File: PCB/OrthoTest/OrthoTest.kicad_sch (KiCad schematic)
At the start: 249 parts, among them SW1 SW_Push, SW10 SW_Push, SW11 SW_Push, SW12 SW_Push, SW13 SW_Push, SW14 SW_Push, SW15 SW_Push, SW16 SW_Push, SW17 SW_Push, SW18 SW_Push, SW19 SW_Push, SW2 SW_Push, SW20 SW_Push, SW21 SW_Push, SW22 SW_Push, SW23 SW_Push, SW24 SW_Push, SW25 SW_Push, SW26 SW_Push, SW27 SW_Push, SW28 SW_Push, SW29 SW_Push, SW3 SW_Push, SW30 SW_Push, SW31 SW_Push, SW32 SW_Push, SW33 SW_Push, SW34 SW_Push, SW35 SW_Push, SW36 SW_Push, SW37 SW_Push, SW38 SW_Push, SW39 SW_Push, SW4 SW_Push, SW40 SW_Push, SW41 SW_Push, SW42 SW_Push, SW43 SW_Push, SW44 SW_Push, SW45 SW_Push, SW46 SW_Push, SW47 SW_Push, SW48 SW_Push, SW49 SW_Push, SW5 SW_Push, SW50 SW_Push, SW51 SW_Push, SW52 SW_Push, SW53 SW_Push, SW54 SW_Push, SW55 SW_Push, SW56 SW_Push, SW57 SW_Push, SW58 SW_Push, SW59 SW_Push, SW6 SW_Push, SW60 RotaryEncoder_Switch_MP, SW61 RotaryEncoder_Switch_MP, SW7 SW_Push, SW8 SW_Push, SW9 SW_Push

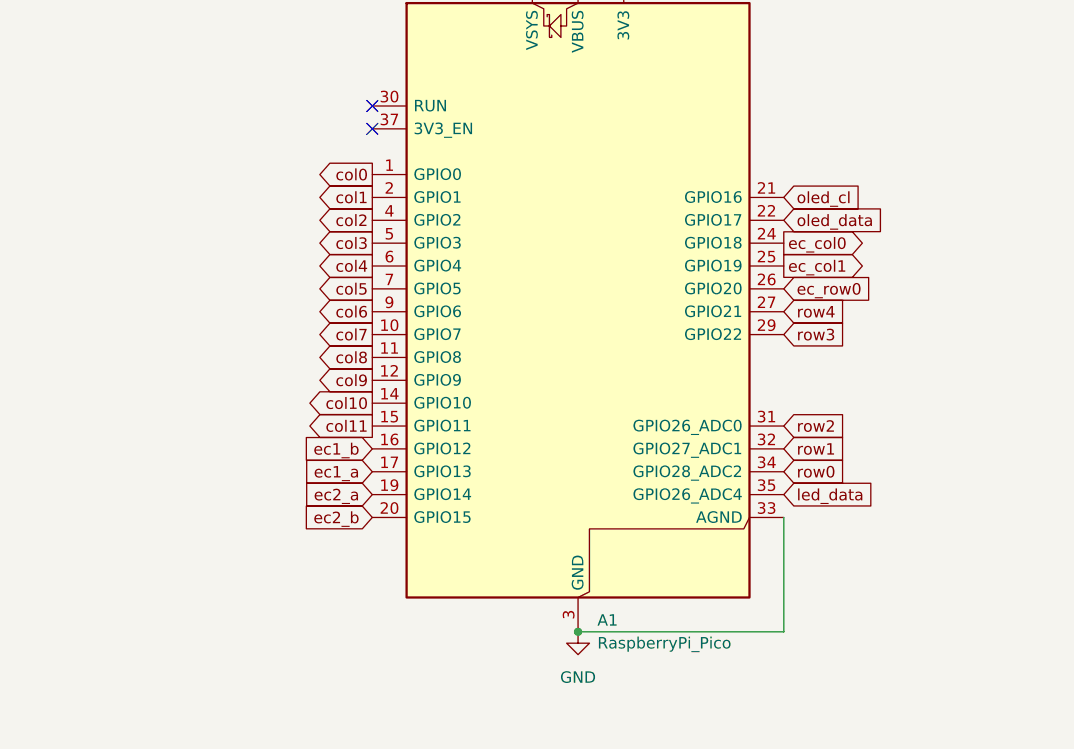
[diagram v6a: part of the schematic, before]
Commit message: rerouting ucontroller
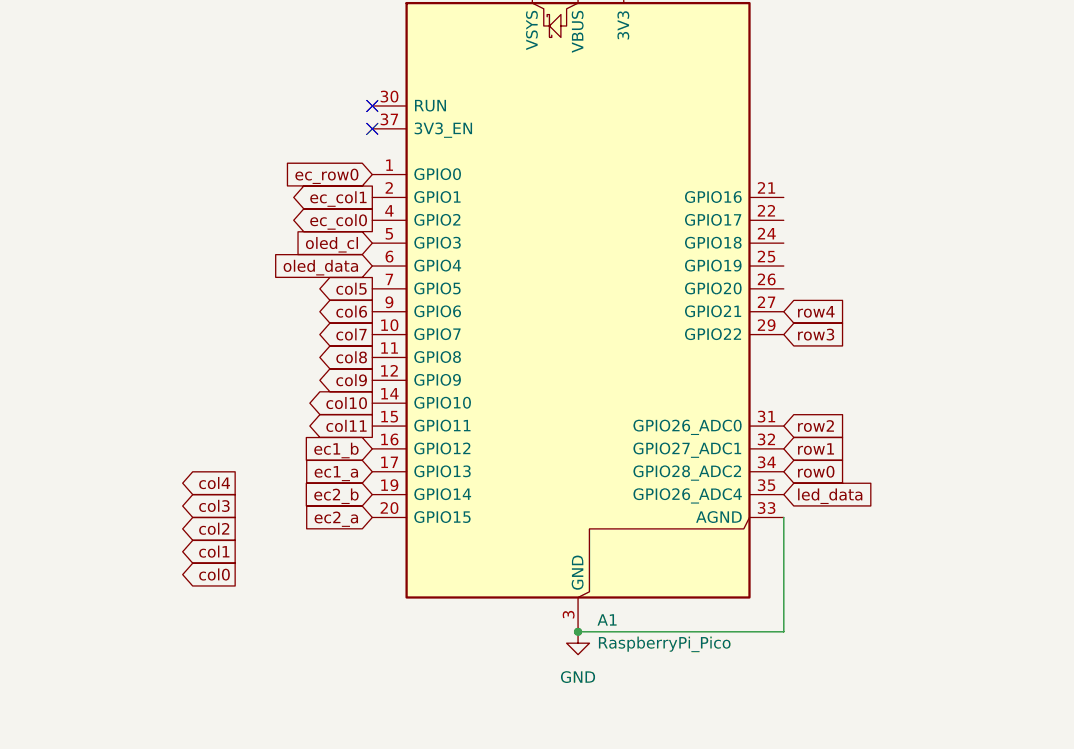
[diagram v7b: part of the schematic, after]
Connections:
- net col0: no longer A1.1 (GPIO0)
- net col1: no longer A1.2 (GPIO1)
- net col2: no longer A1.4 (GPIO2)
- net col3: no longer A1.5 (GPIO3)
- net col4: no longer A1.6 (GPIO4)
- net ec2_a: now also A1.20 (GPIO15); no longer A1.19 (GPIO14)
- net ec2_b: now also A1.19 (GPIO14); no longer A1.20 (GPIO15)
- net ec_col0: now also A1.4 (GPIO2); no longer A1.24 (GPIO18)
- net ec_col1: now also A1.2 (GPIO1); no longer A1.25 (GPIO19)
- net ec_row0: now also A1.1 (GPIO0); no longer A1.26 (GPIO20)
- net oled_cl: now also A1.5 (GPIO3); no longer A1.21 (GPIO16)
- net oled_data: now also A1.6 (GPIO4); no longer A1.22 (GPIO17)

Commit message: added level shifter and finished rerouting
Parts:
- added U5: SN74LVC1T45DCK, Package_TO_SOT_SMD:SOT-363_SC-70-6, symbol Logic_LevelTranslator:SN74LVC1T45DCK
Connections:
- net +3V3: now also U5.1 (VCCA), U5.5 (DIR)
- net +5V: now also U5.6 (VCCB)
- net GND: now also U5.2 (GND)
- net col0: now also A1.34 (GPIO28_ADC2)
- net col1: now also A1.32 (GPIO27_ADC1)
- net col2: now also A1.31 (GPIO26_ADC0)
- net col3: now also A1.29 (GPIO22)
- net col4: now also A1.27 (GPIO21)
- net row0: now also A1.26 (GPIO20); no longer A1.34 (GPIO28_ADC2)
- net row1: now also A1.25 (GPIO19); no longer A1.32 (GPIO27_ADC1)
- net row2: now also A1.24 (GPIO18); no longer A1.31 (GPIO26_ADC0)
- net row3: now also A1.22 (GPIO17); no longer A1.29 (GPIO22)
- net row4: now also A1.21 (GPIO16); no longer A1.27 (GPIO21)
- net led_data renamed led_data_3v3
- net led_data_3v3: now also U5.3 (A); no longer LED1.3 (DIN)
- new net led_data_5v: LED1.3 (DIN), U5.4 (B)
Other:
- note added: "Logic level shifter"
- moved on the sheet: LED1, LED10, LED11, LED12, LED13, LED14, LED15, LED16, LED17, LED18, LED19, LED2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
